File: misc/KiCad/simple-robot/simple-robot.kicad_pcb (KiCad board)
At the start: 4 copper layers, 100 x 100 mm, 70 parts, among them J1 MotLA, J10 Screw_Terminal_2_P5.00mm, J11 JSTHCSR04, J12 IR_RF, J13 IR_LF, J14 JST_GV, J15 JST RF_Logic, J16 JST RF_PW, J2 MotLB, J3 JST03 Servo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

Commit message: fix broken nets on pcb (#38)
swapping of trigger and echo pins was incomplete on pcb nets

update to recent KiCad version
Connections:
- LS_3 pad 5: US_ECHO -> US_TRIG
- LS_3 pad 6: US_TRIG -> US_ECHO
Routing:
- net US_TRIG: track 68.4 -> 64.8 mm
- net US_ECHO: track 64.8 -> 68.4 mm

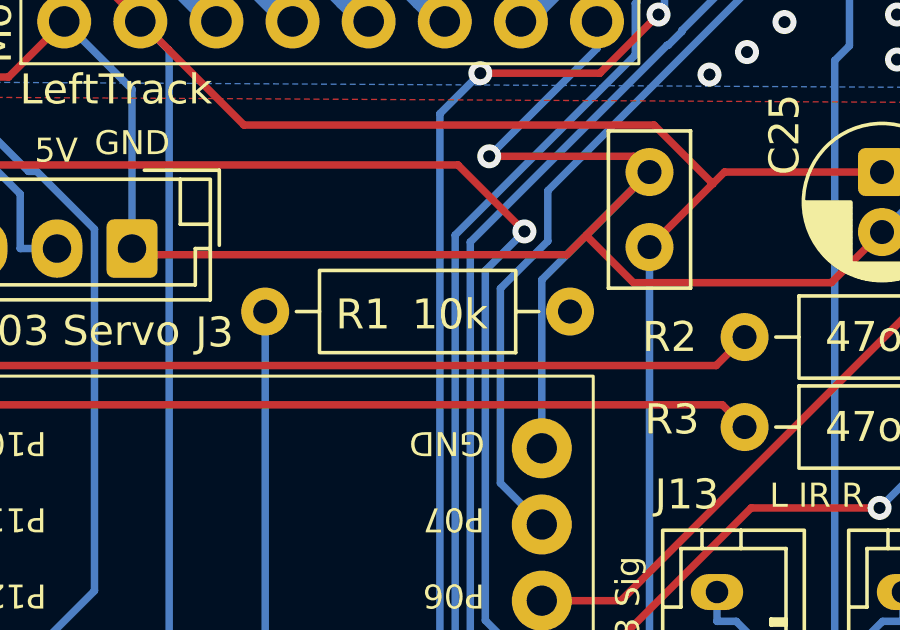
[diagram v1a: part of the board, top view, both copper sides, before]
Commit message: Stabilze obstacle detection (#50)
* Update resistor value from 10k to 3K3 and bump KiCad project revision to
6

* Add coast-avoid detection test and raise obstacle threshold to 20 cm

- Add CoastAvoidDetection test mode to verify
  IR→perception→EmergencyBrake chain
- Raise ultrasonic obstacle threshold from 15 cm to 20 cm for better
  noise margin
- Increase IR signal channel capacity from 4 to 16 to prevent overflow
- Fix obstacle indicator update to always run regardless of change
  detection
- Skip forward drive phase when obstacle already present at startup

* Bump version and update test doc for motor-noise replication

Expand the stationary-test docstring to clarify that motors should
be kept running so the test reproduces the PWM noise environment
encountered during actual coast-avoid driving.
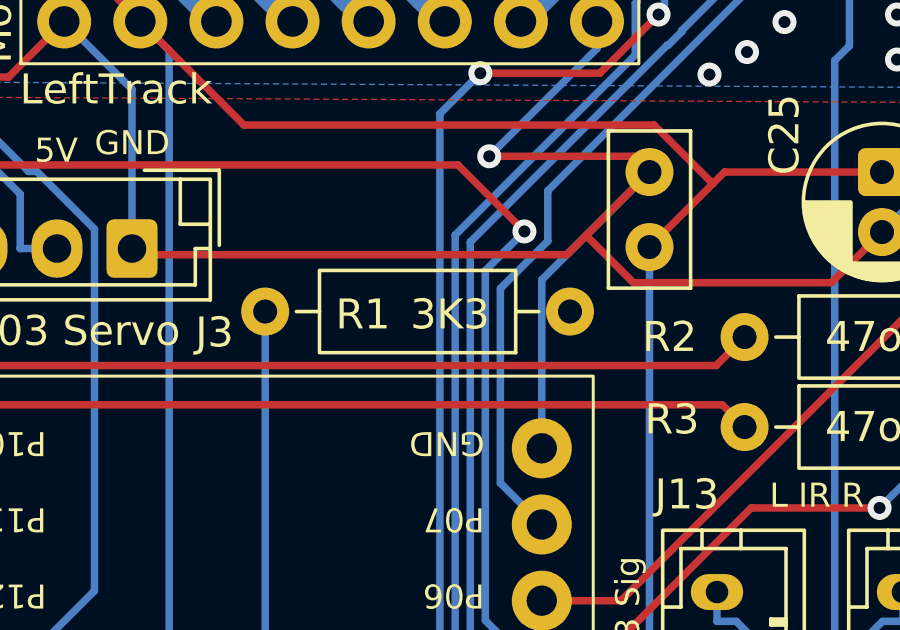
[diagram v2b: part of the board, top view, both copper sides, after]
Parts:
- R1: value 10k -> 3K3
